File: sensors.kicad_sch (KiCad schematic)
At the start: 44 parts, among them J401 ACC_INT1, J402 BME_SPI, J403 LUX_INT, U202 NUCLEO64-H503RB, U401 LSM6DS3, U402 BME280, U403 OPT4001, U404 INA2180A2, U406 YK16S-L7.2-B10Ka(32-8)-G-A29

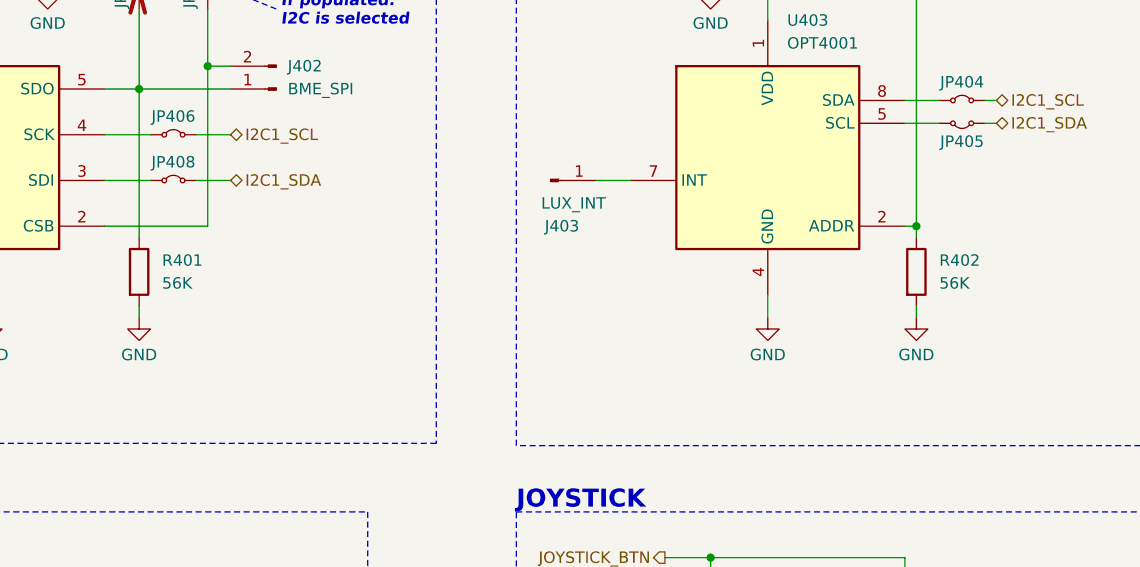
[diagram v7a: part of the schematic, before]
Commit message: added some lcsc PN, and uniformed some resistors values to reduce BOM count
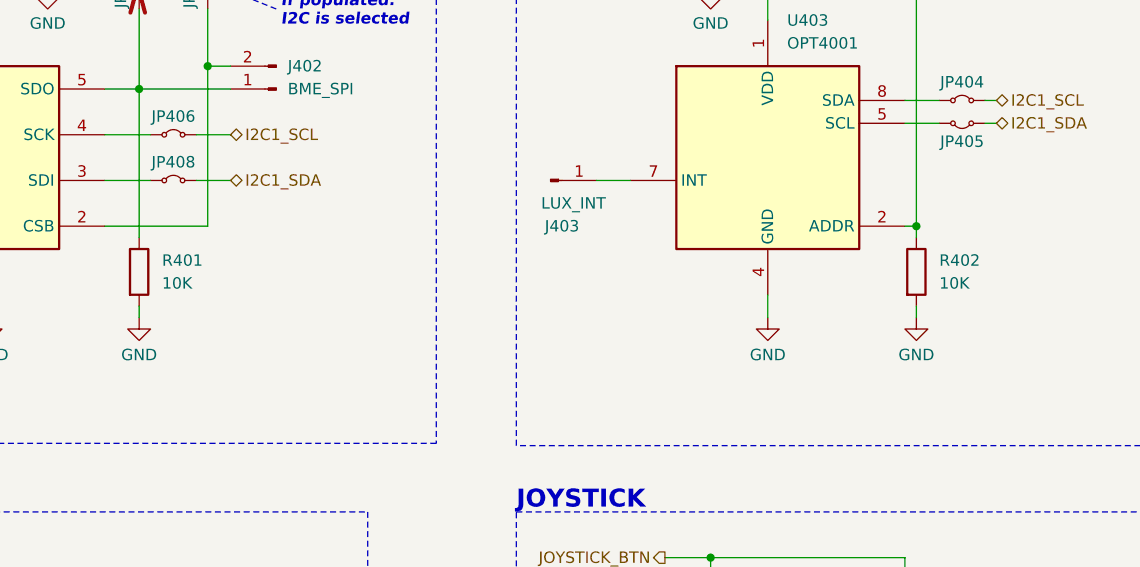
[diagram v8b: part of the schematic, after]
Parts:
- R401, R402: value 56K -> 10K; LCSC C23206 -> C25804
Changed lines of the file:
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@@
 			)
 		)
-		(property "Datasheet" ""
+		(property "Datasheet" "https://jlcpcb.com/api/file/downloadByFileSystemAccessId/8602606255286734848"
 			(at 214.63 59.69 0)
 			(effects
@@
 			)
 		)
-		(property "Value" "56K"
+		(property "Value" "10K"
 			(at 147.32 73.6599 0)
 			(effects
@@
 			)
 		)
-		(property "LCSC" "C23206"
+		(property "LCSC" "C25804"
 			(at 144.78 72.39 0)
 			(effects
@@
 			)
 		)
-		(property "Value" "56K"
+		(property "Value" "10K"
 			(at 233.68 73.6599 0)
 			(effects
@@
 			)
 		)
-		(property "LCSC" "C23206"
+		(property "LCSC" "C25804"
 			(at 231.14 72.39 0)
 			(effects
